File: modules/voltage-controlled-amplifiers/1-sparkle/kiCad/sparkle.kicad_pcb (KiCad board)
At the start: 2 copper layers, 90 x 111 mm, 83 parts, among them J1 OUT_1, J2 IN_1, J3 CV_1, J4 OUT_2, J5 IN_2, J6 CV_2, Q1 BC548, Q2 BC548, Q3 BC548, Q4 BC548, U1 TL074

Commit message: update pcbs and symbols
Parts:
- D1, D2: footprint synth-custom:D_PWR_default -> Synth:D_DO-41_SOD81_P10.16mm_Horizontal
- H1, H4: footprint synth-custom:PinSocket_1x04_P2.54mm_Vertical -> Synth:PinSocket_1x04_P2.54mm_Vertical
- H13: footprint synth-custom:CONN_02x05_PWR -> Synth:IDC-Header_2x05_P2.54mm_Vertical
- H2, H3: footprint synth-custom:PinHeader_1x04_P2.54mm_Vertical -> Synth:PinHeader_1x04_P2.54mm_Vertical
- J1, J2, J3, J4, J5, J6: footprint synth-custom:Jack_default -> Connector_Audio:Jack_3.5mm_QingPu_WQP-PJ398SM_Vertical_CircularHoles
- R1, R10, R11, R12, R13, R14, R15, R16, R17, R18, R19, R2, R20, R21, R22, R23, R24, R25, R26, R27, R28, R29, R3, R30, R31, R32, R33, R34, R4, R5, R6, R7, R8, R9: footprint synth-custom:R_default -> Synth:R_Default (DIN0207)
- moved R16 10.2 mm to (55.0, 100.1), turned to 90 degrees
- moved H13 5.49 mm to (54.9, 67.6), turned to 0 degrees
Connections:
- R16 pad 1: Net-(U1B--) -> Net-(R14-Pad1)
- R16 pad 2: Net-(R14-Pad1) -> Net-(U1B--)
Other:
- board text added: "JLCJLCJLCJLC"
- board text added: "Lenimal PCB Design 04.2024"
- board text added: "SPARKLE"
- board text added: "Voltage Controlled Amplifier"

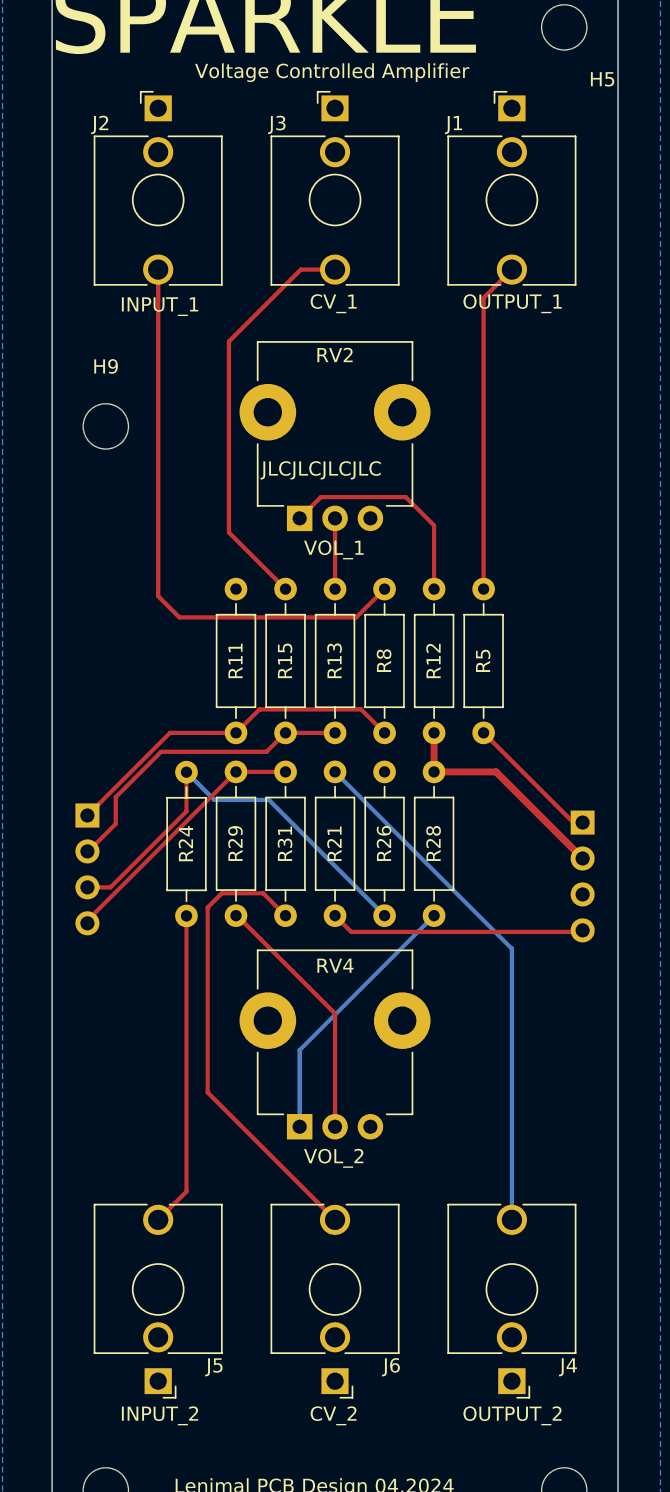
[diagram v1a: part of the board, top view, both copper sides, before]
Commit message: added images and schematics for sparkle, updated footprints and symbols
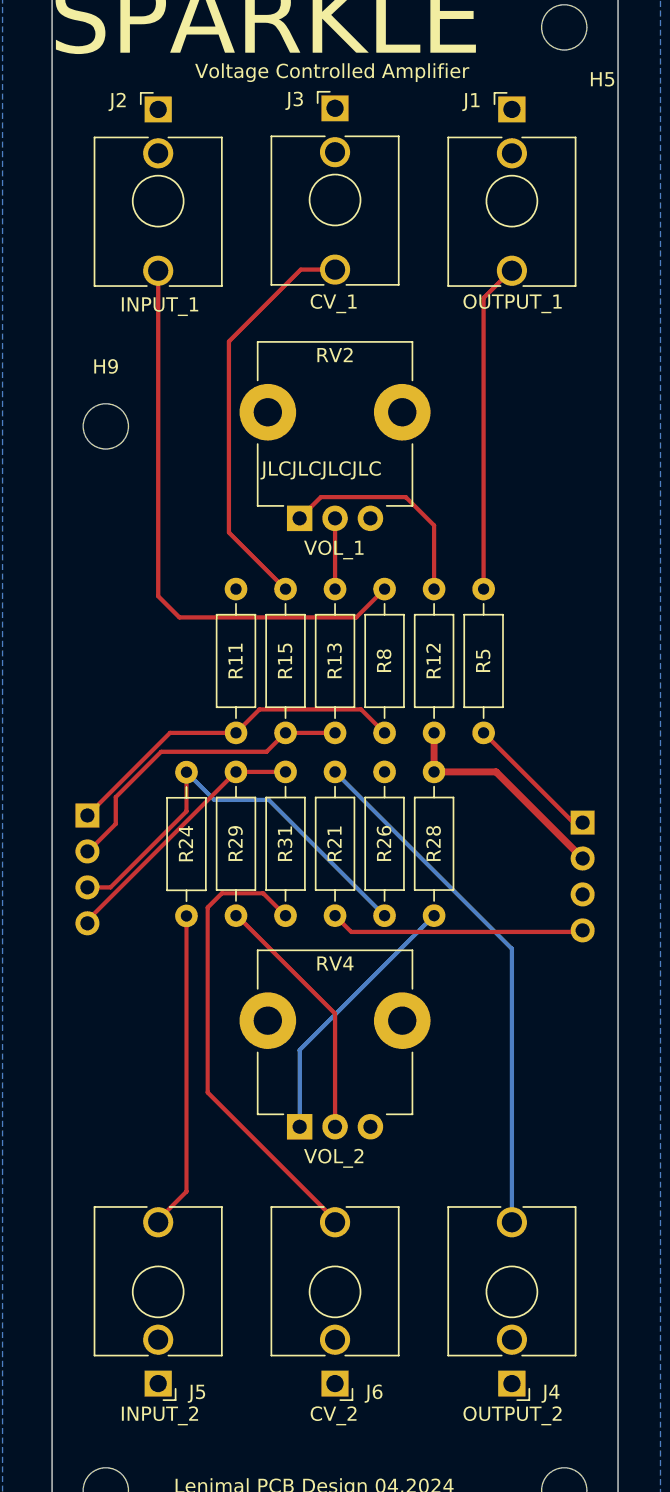
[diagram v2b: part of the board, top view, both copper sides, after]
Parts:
- J1, J2, J3, J4, J5, J6: footprint Connector_Audio:Jack_3.5mm_QingPu_WQP-PJ398SM_Vertical_CircularHoles -> Synth:Jack_3.5mm_QingPu_WQP-PJ398SM_Vertical_CircularHoles
- RV2, RV4: footprint Potentiometer_THT:Potentiometer_TT_P0915N -> Synth:Potentiometer_TT_P0915N
- moved RV2 7.91 mm to (120.0, 81.0)
- moved RV4 7.91 mm to (120.0, 124.0)
- moved J1 6.56 mm to (132.5, 66.1)
- moved J2 6.56 mm to (107.5, 66.1)
- moved J3 6.48 mm to (120.0, 66.0)
- moved J4 6.31 mm to (132.5, 143.2)
- moved J5 6.31 mm to (107.5, 143.2)
- moved J6 6.31 mm to (120.0, 143.2)

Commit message: add gerber files and ZIPs for V2
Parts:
- moved H2 9.00 mm to (128.5, 110.0)
- moved H3 9.00 mm to (93.5, 109.5)
- moved H6 9.00 mm to (94.8, 157.2)
- moved H9 9.00 mm to (94.8, 82.0)
- moved J1 9.00 mm to (123.5, 66.1)
- moved J2 9.00 mm to (98.5, 66.1)
- moved J3 9.00 mm to (111.0, 66.0)
- moved J4 9.00 mm to (123.5, 143.2)
- moved J5 9.00 mm to (98.5, 143.2)
- moved J6 9.00 mm to (111.0, 143.2)
- moved R11 9.00 mm to (104.0, 93.5)
- moved R12 9.00 mm to (118.0, 93.5)
- moved R13 9.00 mm to (111.0, 93.5)
- moved R15 9.00 mm to (107.5, 93.5)
- moved R21 9.00 mm to (111.0, 116.6)
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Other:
- board size 90 x 111 mm -> 81 x 111 mm
- board text added: "In the rack, a sparkle ignites, Voltage whispers, in the night. Amplifier, with power to soar, Sparkle's glow, forevermore."
- board text added: "Voltage flows, controlled and true, Sparkle's touch, a sonic hue. In every note, her brilliance gleams, Amplifying dreams, to realms unseen."

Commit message: cleaning up the main readme, update for 3340-vco
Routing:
- added copper zone on F.Cu, net (none)
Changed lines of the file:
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@@
+	)
+	(zone
+		(net 0)
+		(net_name "")
+		(layer "F.Cu")
+		(hatch edge 0.5)
+		(priority 1)
+		(connect_pads
+			(clearance 0.5)
+		)
+		(min_thickness 0.25)
+		(filled_areas_thickness no)
+		(fill yes
+			(thermal_gap 0.5)
+			(thermal_bridge_width 0.5)
+			(island_removal_mode 1)
+			(island_area_min 10)
+		)
+		(polygon
+			(pts
+				(xy 45 45) (xy 135 45) (xy 135 165) (xy 45 165)
+			)
+		)
 	)
 	(zone

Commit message: final versions of PCB for modules
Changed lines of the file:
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@@
-		)
-	)
-	(gr_text "JLCJLCJLCJLC"
-		(at 105.8 85.6 0)
-		(layer "F.SilkS")
-		(effects
-			(font
-				(size 1 1)
-				(thickness 0.15)
-			)
-			(justify left bottom)
 		)
 	)
